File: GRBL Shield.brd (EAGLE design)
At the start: 94.9 x 80 mm, 38 parts

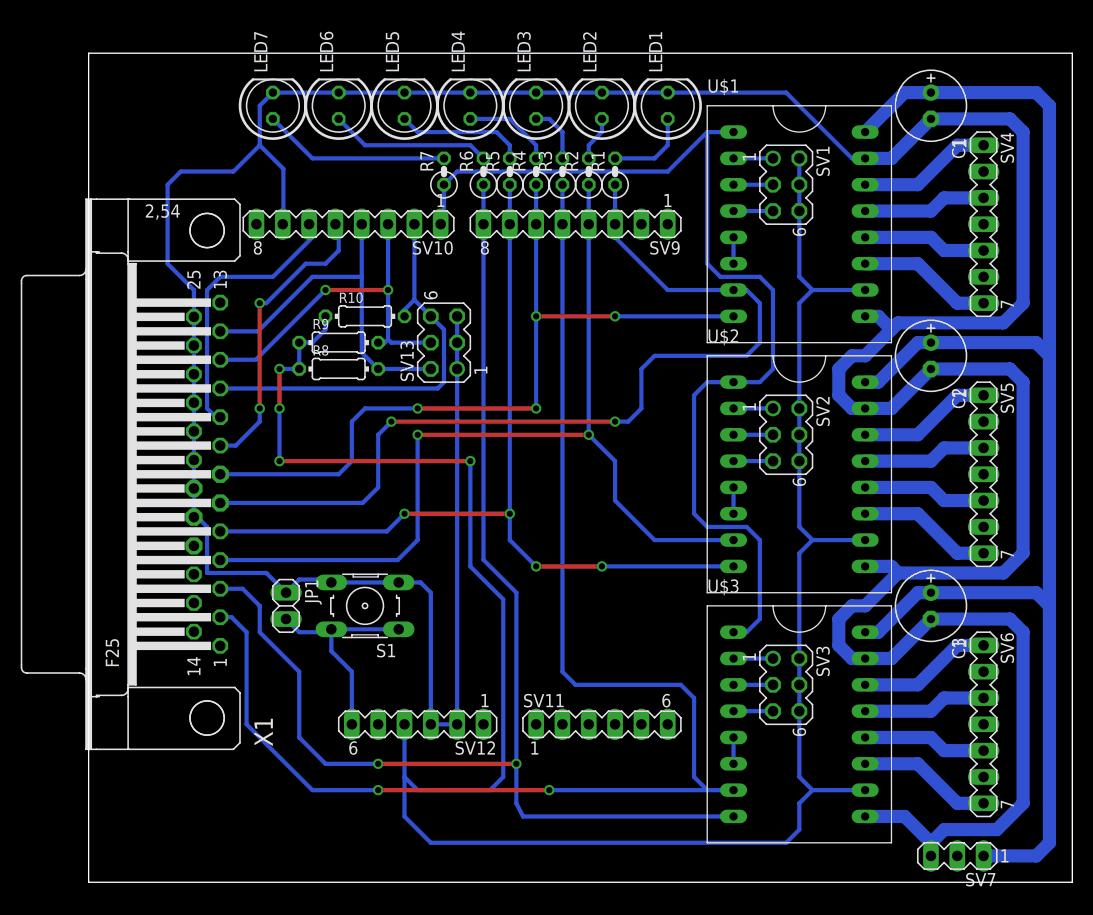
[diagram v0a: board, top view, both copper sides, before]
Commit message: Added values for components and added 5V regulator #1
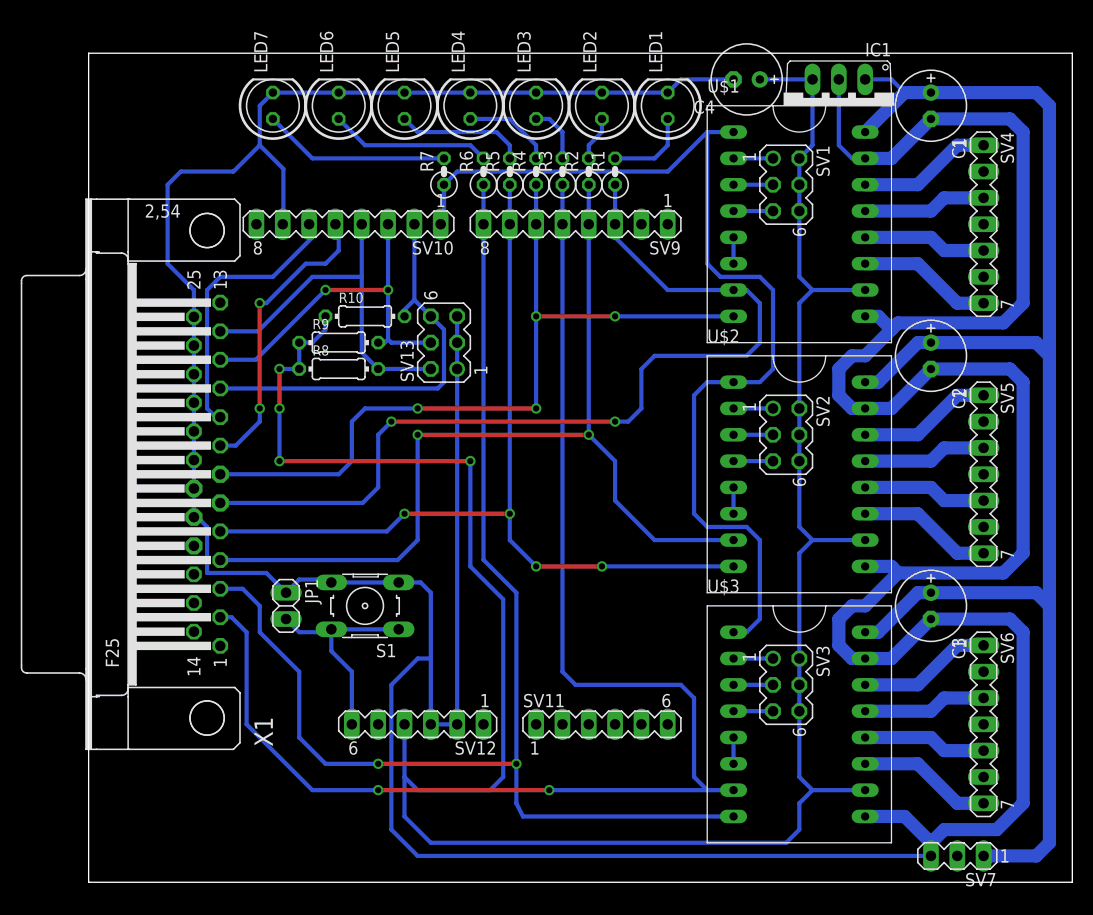
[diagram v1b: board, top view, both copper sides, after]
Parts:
- added C4: 100uf, rcl:E2,5-7
- added IC1: 7805, linear:TO220V
- C1, C2, C3: value (none) -> 100uf
- LED1, LED4: value (none) -> RED
- LED2, LED5: value (none) -> GRN
- LED3, LED6: value (none) -> YLW
- LED7: value (none) -> BLU
- R1, R2, R3, R4, R5, R6: value (none) -> 150R
- R10, R8, R9: value (none) -> 10k
- R7: value (none) -> 68R
- SV10: value (none) -> 8-13/GND/AREF
- SV11: value (none) -> A0-A5
- SV12: value (none) -> RST/3.3/5/GND/GND/VIN
- SV9: value (none) -> 0-7
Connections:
- net +24V: now also IC1.1
- net +5V: now also C4.+, IC1.3
- net GND: now also C4.-, IC1.2
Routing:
- net GND: track 380.9 -> 447.5 mm
- net +5V: track 210.2 -> 223.4 mm
- net +24V: track 137.6 -> 142.0 mm
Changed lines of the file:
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@@
 <attribute name="OC_FARNELL" value="unknown" x="29.21" y="105.41" size="1.778" layer="27" rot="R180" display="off"/>
 </element>
-<element name="LED1" library="led" package="LED5MM" value="" x="55.88" y="74.93" rot="R90"/>
-<element name="LED2" library="led" package="LED5MM" value="" x="49.53" y="74.93" rot="R90"/>
-<element name="LED3" library="led" package="LED5MM" value="" x="43.18" y="74.93" rot="R90"/>
-<element name="LED4" library="led" package="LED5MM" value="" x="36.83" y="74.93" rot="R90"/>
-<element name="LED5" library="led" package="LED5MM" value="" x="30.48" y="74.93" rot="R90"/>
-<element name="LED6" library="led" package="LED5MM" value="" x="24.13" y="74.93" rot="R90"/>
-<element name="R1" library="rcl" package="0207/2V" value="" x="50.8" y="68.58" rot="R90"/>
-<element name="R2" library="rcl" package="0207/2V" value="" x="48.26" y="68.58" rot="R90"/>
-<element name="R3" library="rcl" package="0207/2V" value="" x="45.72" y="68.58" rot="R90"/>
-<element name="R4" library="rcl" package="0207/2V" value="" x="43.18" y="68.58" rot="R90"/>
-<element name="R5" library="rcl" package="0207/2V" value="" x="40.64" y="68.58" rot="R90"/>
-<element name="R6" library="rcl" package="0207/2V" value="" x="38.1" y="68.58" rot="R90"/>
-<element name="LED7" library="led" package="LED5MM" value="" x="17.78" y="74.93" rot="R90"/>
-<element name="R7" library="rcl" package="0207/2V" value="" x="34.29" y="68.58" rot="R90"/>
-<element name="C1" library="rcl" package="E2,5-7" value="" x="81.28" y="74.93" rot="R270"/>
-<element name="C2" library="rcl" package="E2,5-7" value="" x="81.28" y="50.8" rot="R270"/>
-<element name="C3" library="rcl" package="E2,5-7" value="" x="81.28" y="26.67" rot="R270"/>
+<element name="LED1" library="led" package="LED5MM" value="RED" x="55.88" y="74.93" rot="R90"/>
+<element name="LED2" library="led" package="LED5MM" value="GRN" x="49.53" y="74.93" rot="R90"/>
+<element name="LED3" library="led" package="LED5MM" value="YLW" x="43.18" y="74.93" rot="R90"/>
+<element name="LED4" library="led" package="LED5MM" value="RED" x="36.83" y="74.93" rot="R90"/>
+<element name="LED5" library="led" package="LED5MM" value="GRN" x="30.48" y="74.93" rot="R90"/>
+<element name="LED6" library="led" package="LED5MM" value="YLW" x="24.13" y="74.93" rot="R90"/>
+<element name="R1" library="rcl" package="0207/2V" value="150R" x="50.8" y="68.58" rot="R90"/>
+<element name="R2" library="rcl" package="0207/2V" value="150R" x="48.26" y="68.58" rot="R90"/>
+<element name="R3" library="rcl" package="0207/2V" value="150R" x="45.72" y="68.58" rot="R90"/>
+<element name="R4" library="rcl" package="0207/2V" value="150R" x="43.18" y="68.58" rot="R90"/>
+<element name="R5" library="rcl" package="0207/2V" value="150R" x="40.64" y="68.58" rot="R90"/>
+<element name="R6" library="rcl" package="0207/2V" value="150R" x="38.1" y="68.58" rot="R90"/>
+<element name="LED7" library="led" package="LED5MM" value="BLU" x="17.78" y="74.93" rot="R90"/>
+<element name="R7" library="rcl" package="0207/2V" value="68R" x="34.29" y="68.58" rot="R90"/>
+<element name="C1" library="rcl" package="E2,5-7" value="100uf" x="81.28" y="74.93" rot="R270"/>
+<element name="C2" library="rcl" package="E2,5-7" value="100uf" x="81.28" y="50.8" rot="R270"/>
+<element name="C3" library="rcl" package="E2,5-7" value="100uf" x="81.28" y="26.67" rot="R270"/>
 <element name="S1" library="switch-omron" package="B3F-10XX" value="" x="26.67" y="26.67" rot="R180">
 <attribute name="OC_NEWARK" value="36M3542" x="26.67" y="26.67" size="2.54" layer="27" rot="R180" display="off"/>
@@
 <attribute name="OC_FARNELL" value="unknown" x="11.43" y="39.37" size="1.778" layer="27" rot="R90" display="off"/>
 </element>
-<element name="SV9" library="con-lstb" package="MA08-1" value="" x="46.99" y="63.5" rot="R180">
+<element name="SV9" library="con-lstb" package="MA08-1" value="0-7" x="46.99" y="63.5" rot="R180">
 <attribute name="OC_NEWARK" value="unknown" x="46.99" y="63.5" size="1.778" layer="27" rot="R180" display="off"/>
 <attribute name="MPN" value="" x="46.99" y="63.5" size="1.778" layer="27" rot="R180" display="off"/>
@@
 <attribute name="OC_FARNELL" value="unknown" x="46.99" y="63.5" size="1.778" layer="27" rot="R180" display="off"/>
 </element>
-<element name="SV10" library="con-lstb" package="MA08-1" value="" x="25.0825" y="63.5" rot="R180">
+<element name="SV10" library="con-lstb" package="MA08-1" value="8-13/GND/AREF" x="25.0825" y="63.5" rot="R180">
 <attribute name="OC_NEWARK" value="unknown" x="25.0825" y="63.5" size="1.778" layer="27" rot="R180" display="off"/>
 <attribute name="MPN" value="" x="25.0825" y="63.5" size="1.778" layer="27" rot="R180" display="off"/>
@@
 <attribute name="OC_FARNELL" value="unknown" x="25.0825" y="63.5" size="1.778" layer="27" rot="R180" display="off"/>
 </element>
-<element name="SV11" library="con-lstb" package="MA06-1" value="" x="49.53" y="15.24">
+<element name="SV11" library="con-lstb" package="MA06-1" value="A0-A5" x="49.53" y="15.24">
 <attribute name="OC_NEWARK" value="unknown" x="49.53" y="15.24" size="1.778" layer="27" display="off"/>
 <attribute name="MPN" value="" x="49.53" y="15.24" size="1.778" layer="27" display="off"/>
@@
 <attribute name="OC_FARNELL" value="unknown" x="49.53" y="15.24" size="1.778" layer="27" display="off"/>
 </element>
-<element name="SV12" library="con-lstb" package="MA06-1" value="" x="31.75" y="15.24" rot="R180">
+<element name="SV12" library="con-lstb" package="MA06-1" value="RST/3.3/5/GND/GND/VIN" x="31.75" y="15.24" rot="R180">
 <attribute name="OC_NEWARK" value="unknown" x="31.75" y="15.24" size="1.778" layer="27" rot="R180" display="off"/>
 <attribute name="MPN" value="" x="31.75" y="15.24" size="1.778" layer="27" rot="R180" display="off"/>
@@
 <attribute name="OC_FARNELL" value="unknown" x="34.29" y="52.07" size="1.778" layer="27" rot="R90" display="off"/>
 </element>
-<element name="R8" library="rcl" package="0204/7" value="" x="24.13" y="49.53"/>
-<element name="R9" library="rcl" package="0204/7" value="" x="24.13" y="52.07"/>
-<element name="R10" library="rcl" package="0204/7" value="" x="26.67" y="54.61"/>
+<element name="R8" library="rcl" package="0204/7" value="10k" x="24.13" y="49.53"/>
+<element name="R9" library="rcl" package="0204/7" value="10k" x="24.13" y="52.07"/>
+<element name="R10" library="rcl" package="0204/7" value="10k" x="26.67" y="54.61"/>
+<element name="IC1" library="linear" package="TO220V" value="7805" x="72.39" y="74.93" rot="R180"/>
+<element name="C4" library="rcl" package="E2,5-7" value="100uf" x="63.5" y="77.47" rot="R180"/>
 </elements>
 <signals>
@@
 <via x="18.415" y="49.53" extent="1-16" drill="0.6" diameter="1.016"/>
 <wire x1="18.415" y1="49.53" x2="20.32" y2="49.53" width="0.4064" layer="16"/>
+<contactref element="IC1" pad="3"/>
+<contactref element="C4" pad="+"/>
+<wire x1="68.58" y1="69.85" x2="69.85" y2="71.12" width="0.4064" layer="16"/>
+<wire x1="69.85" y1="71.12" x2="69.85" y2="77.47" width="0.4064" layer="16"/>
+<wire x1="69.85" y1="77.47" x2="64.77" y2="77.47" width="0.4064" layer="16"/>
 </signal>
 <signal name="GND">
@@
 <wire x1="74.93" y1="69.85" x2="77.47" y2="69.85" width="1.27" layer="16"/>
 <wire x1="77.47" y1="69.85" x2="81.28" y2="73.66" width="1.27" layer="16"/>
-<wire x1="55.88" y1="76.2" x2="67.31" y2="76.2" width="0.4064" layer="16"/>
-<wire x1="67.31" y1="76.2" x2="73.66" y2="69.85" width="0.4064" layer="16"/>
-<wire x1="73.66" y1="69.85" x2="74.93" y2="69.85" width="0.4064" layer="16"/>
 <wire x1="74.93" y1="21.59" x2="73.66" y2="21.59" width="1.27" layer="16"/>
 <wire x1="73.66" y1="21.59" x2="72.39" y2="22.86" width="1.27" layer="16"/>
@@
 <contactref element="S1" pad="4"/>
 <contactref element="JP1" pad="1"/>
-<wire x1="33.02" y1="27.94" x2="33.02" y2="15.24" width="0.4064" layer="16"/>
+<wire x1="33.02" y1="27.94" x2="33.02" y2="21.59" width="0.4064" layer="16"/>
+<wire x1="33.02" y1="21.59" x2="33.02" y2="15.24" width="0.4064" layer="16"/>
 <wire x1="19.05" y1="27.94" x2="20.32" y2="29.21" width="0.4064" layer="16"/>
 <wire x1="20.32" y1="29.21" x2="23.1394" y2="29.21" width="0.4064" layer="16"/>
@@
 <wire x1="35.56" y1="52.07" x2="35.56" y2="54.61" width="0.4064" layer="16"/>
 <wire x1="35.56" y1="49.53" x2="35.56" y2="15.24" width="0.4064" layer="16"/>
+<contactref element="IC1" pad="2"/>
+<contactref element="C4" pad="-"/>
+<wire x1="72.39" y1="77.47" x2="72.39" y2="71.12" width="0.4064" layer="16"/>
+<wire x1="72.39" y1="71.12" x2="73.66" y2="69.85" width="0.4064" layer="16"/>
+<wire x1="73.66" y1="69.85" x2="74.93" y2="69.85" width="0.4064" layer="16"/>
+<wire x1="62.23" y1="77.47" x2="57.15" y2="77.47" width="0.4064" layer="16"/>
+<wire x1="57.15" y1="77.47" x2="55.88" y2="76.2" width="0.4064" layer="16"/>
+<wire x1="33.02" y1="21.59" x2="31.75" y2="21.59" width="0.4064" layer="16"/>
+<wire x1="31.75" y1="21.59" x2="29.21" y2="19.05" width="0.4064" layer="16"/>
+<wire x1="29.21" y1="19.05" x2="29.21" y2="5.08" width="0.4064" layer="16"/>
+<wire x1="29.21" y1="5.08" x2="31.75" y2="2.54" width="0.4064" layer="16"/>
+<wire x1="31.75" y1="2.54" x2="81.28" y2="2.54" width="0.4064" layer="16"/>
 <wire x1="18.796" y1="63.5" x2="18.7325" y2="63.5" width="0" layer="19" extent="16-16"/>
 </signal>
@@
 <wire x1="92.71" y1="74.93" x2="91.44" y2="76.2" width="1.27" layer="16"/>
 <wire x1="91.44" y1="76.2" x2="81.28" y2="76.2" width="1.27" layer="16"/>
+<contactref element="IC1" pad="1"/>
+<wire x1="74.93" y1="77.47" x2="77.47" y2="77.47" width="0.4064" layer="16"/>
+<wire x1="77.47" y1="77.47" x2="78.74" y2="76.2" width="0.4064" layer="16"/>
 </signal>
 <signal name="N$39">
